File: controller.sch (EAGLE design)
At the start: 53 parts, among them IC1 7805DT, Q1 MOSFET_PCHANNEL, Q2 MOSFET-NCHANNELBSS123LT1G, Q3 MOSFET-NCHANNELFDD8780, U1 ATMEGA328P, Y1 16MHz

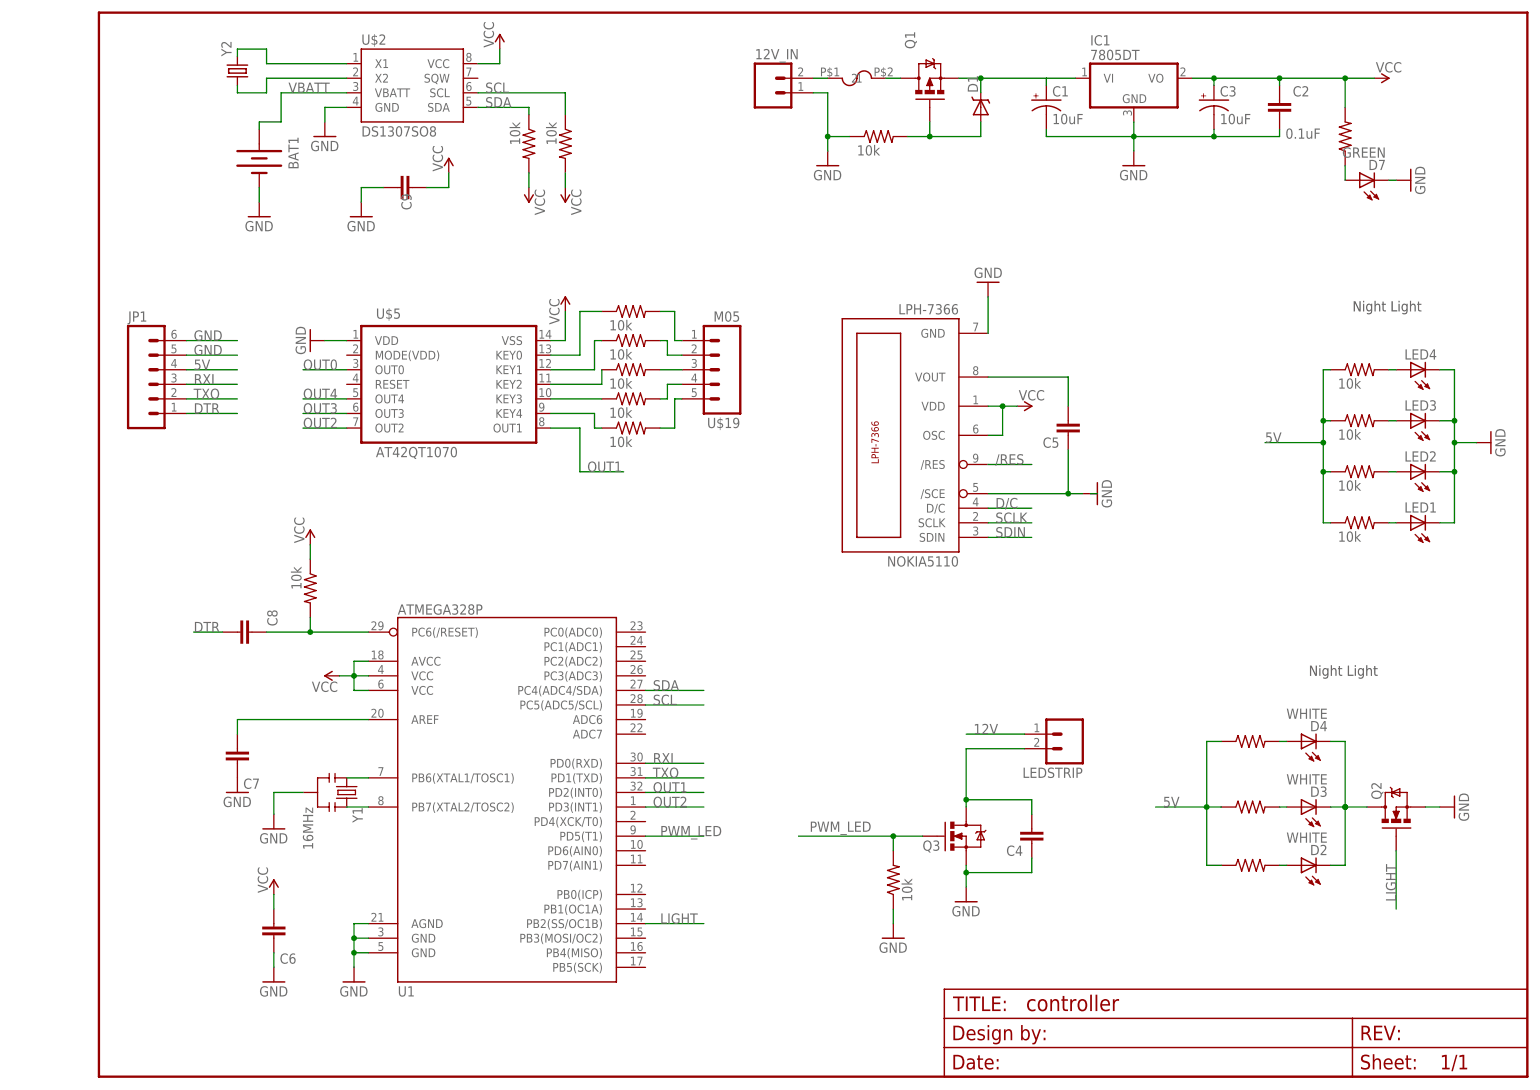
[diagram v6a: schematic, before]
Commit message: compacted layout. rerouted rtc. routed cap IC.
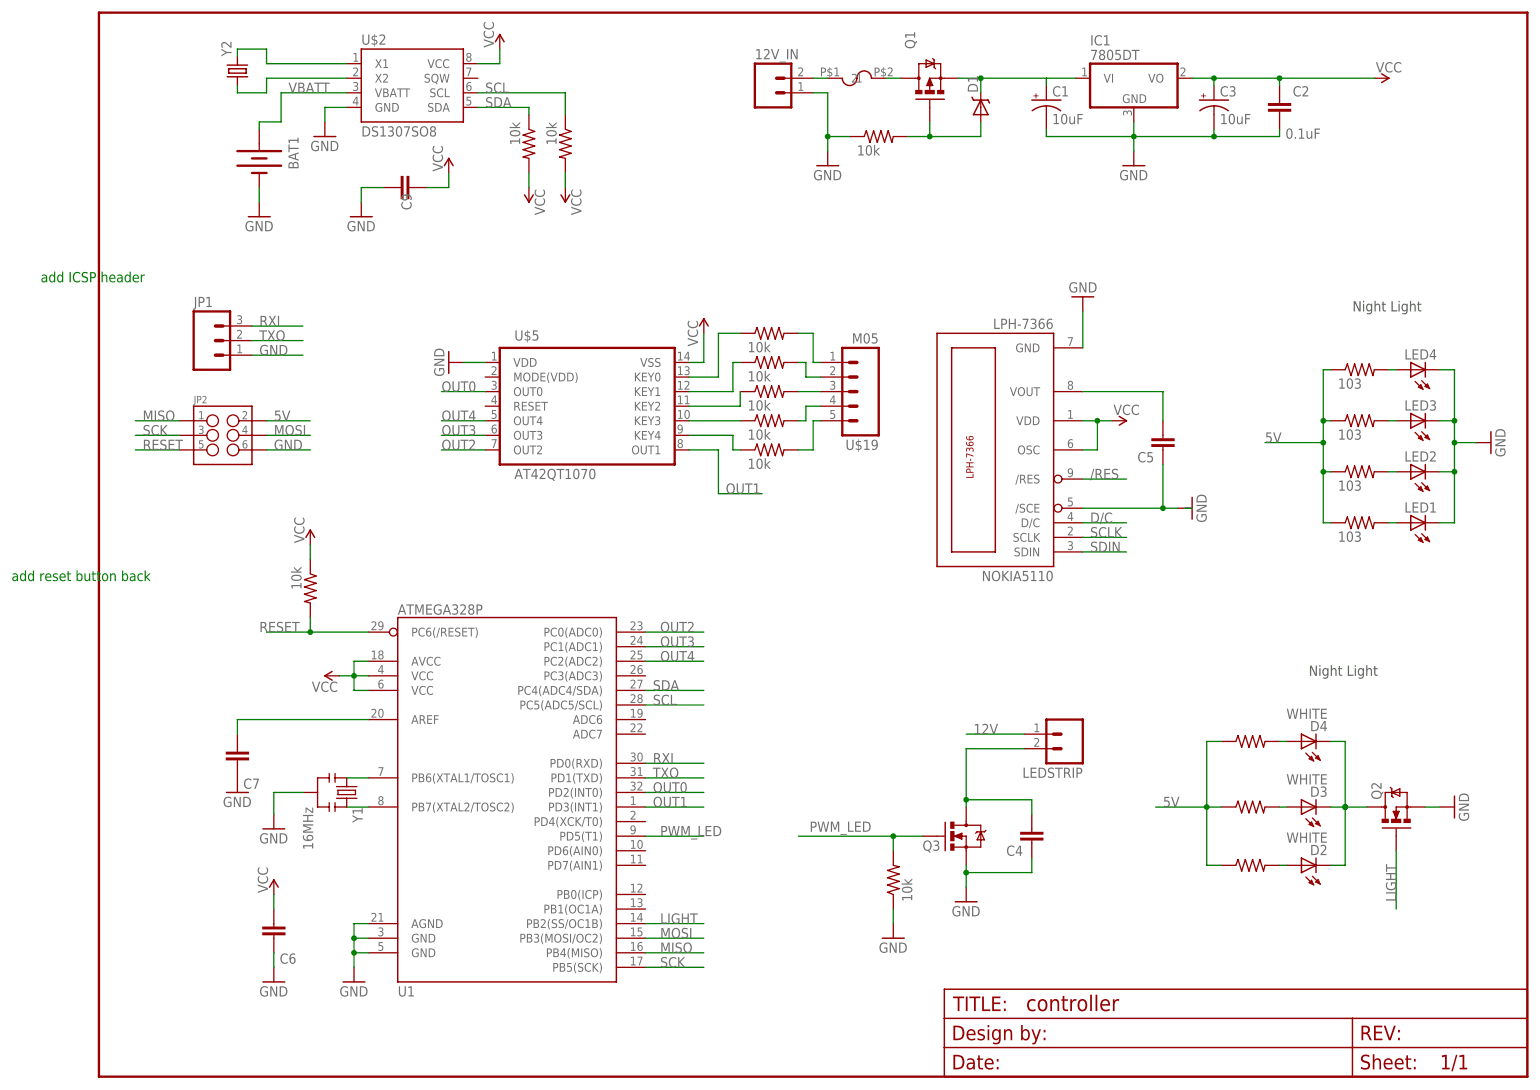
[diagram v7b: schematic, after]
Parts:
- removed C8: (no value), SparkFun-Capacitors:CAP0805
- removed D7: GREEN, SparkFun-LED:LED-GREENLARGE
- removed U$4: (no value), jt_parts:RESISTOR
- added JP2: (no value), SparkFun-Connectors:M03X2POGO_PINS
- JP1: device SparkFun-Connectors:M06POGOPIN_HOLES_ONLY -> SparkFun-Connectors:M03POGO_PIN_HOLES_ONLY
- U$18, U$21, U$22, U$6: value 10k -> 103
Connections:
- removed net DTR: C8.1, JP1.1
- removed net N$10: D7.A, U$4.1
- removed net N$15: C8.2, U$8.2, U1.PC6(/RESET)
- removed net VCC: NOKIA5110.OSC, NOKIA5110.VDD, U$10.2, U$9.2
- new net MISO: JP2.1, U1.PB4(MISO)
- new net MOSI: JP2.4, U1.PB3(MOSI/OC2)
- new net RESET: JP2.5, U$8.2, U1.PC6(/RESET)
- new net SCK: JP2.3, U1.PB5(SCK)
- net 5V: now also JP2.2, NOKIA5110.OSC, NOKIA5110.VDD, U$10.2, U$9.2; no longer JP1.4, U$4.2
- net GND: now also JP1.1, JP2.6; no longer D7.C, JP1.5, JP1.6
- net OUT0: now also U1.PD2(INT0)
- net OUT1: now also U1.PD3(INT1); no longer U1.PD2(INT0)
- net OUT2: now also U1.PC0(ADC0); no longer U1.PD3(INT1)
- net OUT3: now also U1.PC1(ADC1)
- net OUT4: now also U1.PC2(ADC2)
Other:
- note added: "add ICSP header"
- note added: "add reset button back"
- moved on the sheet: C5, NOKIA5110, U$19, U$5

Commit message: put leds in series. continue to tweak layout.
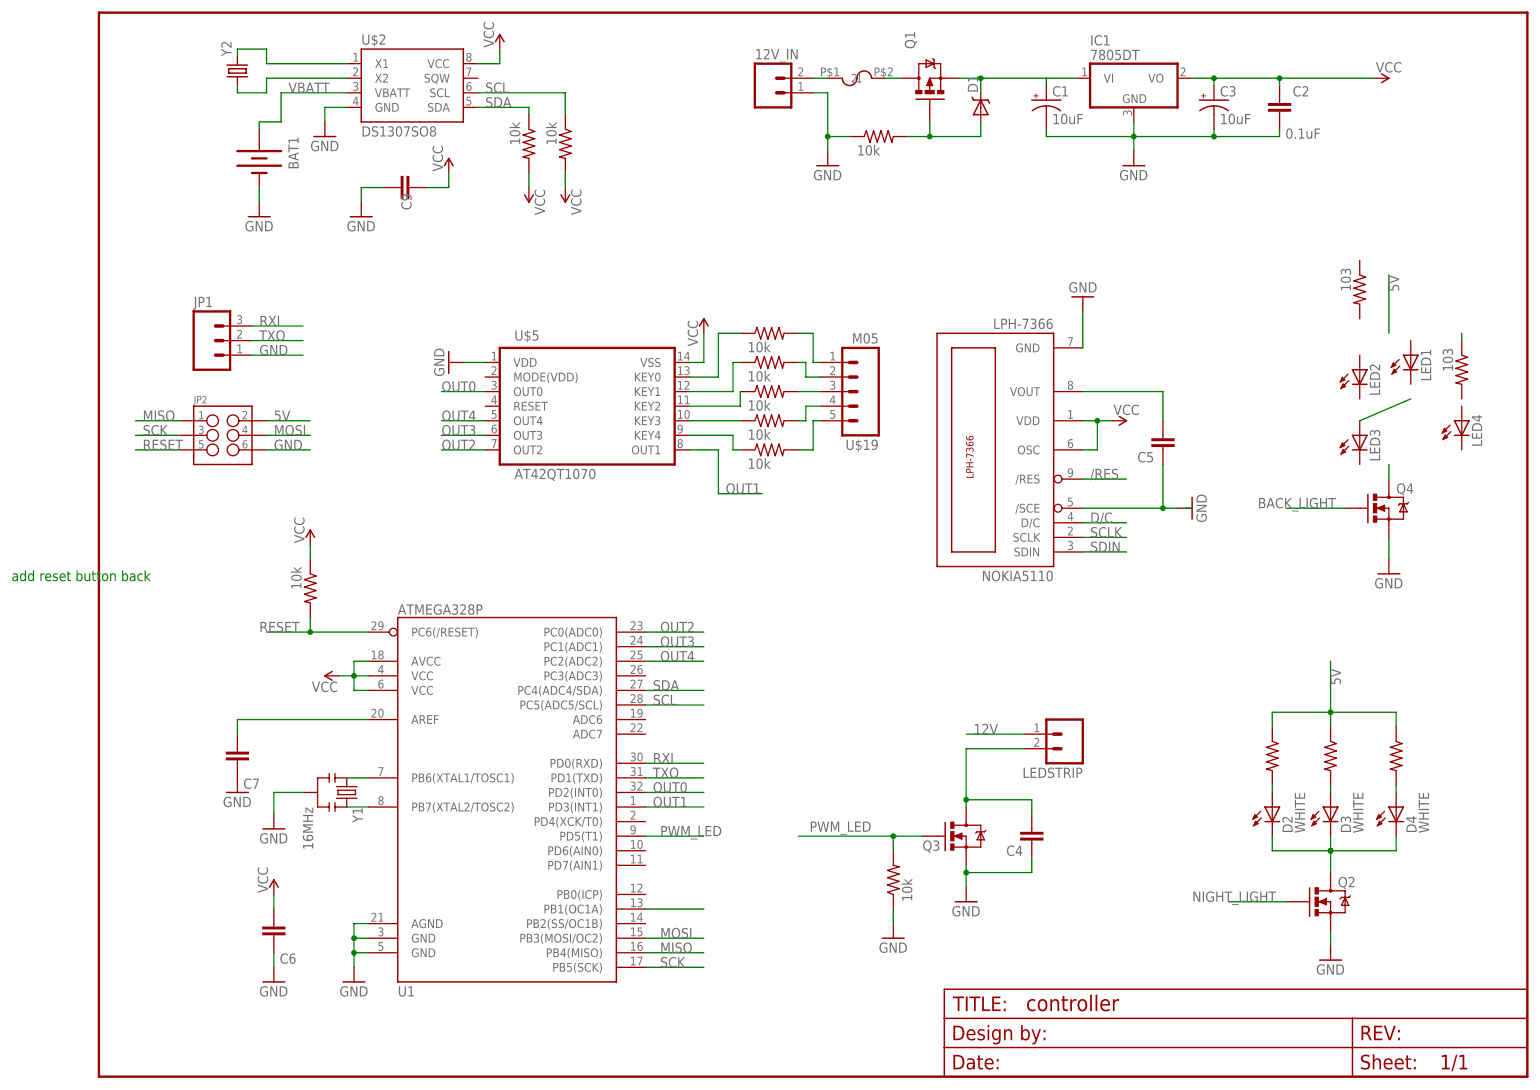
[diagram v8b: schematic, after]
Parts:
- removed U$18, U$22: 103, jt_parts:RESISTOR
- added Q4: MOSFET-NCHANNELBSS123LT1G, SparkFun-DiscreteSemi:MOSFET-NCHANNELBSS123LT1G
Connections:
- removed net LIGHT: Q2.G, U1.PB2(SS/OC1B)
- removed net N$22: LED4.A, U$6.2
- removed net N$34: LED2.A, U$21.2
- removed net N$35: LED1.A, U$22.2
- new net BACK_LIGHT: Q4.G, U1.PB1(OC1A)
- new net N$10: Q4.D
- new net N$5: U$6.1
- new net NIGHT_LIGHT: Q2.G
- net 5V: no longer U$18.1, U$21.1, U$22.1, U$6.1
- net GND: now also Q4.S; no longer LED1.C, LED2.C, LED3.C, LED4.C
- net N$33: no longer U$18.2
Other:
- note removed: "Night Light"
- note removed: "add ICSP header"
- moved on the sheet: D2, D3, D4, LED1, LED2, LED3, LED4, Q2
